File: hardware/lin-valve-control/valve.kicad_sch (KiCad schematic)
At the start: 15 parts, among them J4 Screw_Terminal_01x05, U5 TCA9534, U6 DRV8801PWP

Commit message: Add PCA9536 for the LINBus Address
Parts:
- renumbered U5 to U6, U6 to U7
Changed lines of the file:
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@@
   (symbol (lib_id "power:+3V3") (at 144.526 35.306 0) (unit 1)
     (in_bom yes) (on_board yes) (fields_autoplaced)
-    (property "Reference" "#PWR044" (id 0) (at 144.526 39.116 0)
+    (property "Reference" "#PWR047" (id 0) (at 144.526 39.116 0)
       (effects (font (size 1.27 1.27)) hide)
     )
@@
   (symbol (lib_id "Interface_Expansion:TCA9534") (at 122.047 58.293 0) (unit 1)
     (in_bom yes) (on_board yes) (fields_autoplaced)
-    (property "Reference" "U5" (id 0) (at 124.0664 41.91 0)
+    (property "Reference" "U6" (id 0) (at 124.0664 41.91 0)
       (effects (font (size 1.27 1.27)) (justify left))
     )
@@
   (symbol (lib_id "power:+3V3") (at 101.473 104.775 0) (unit 1)
     (in_bom yes) (on_board yes) (fields_autoplaced)
-    (property "Reference" "#PWR038" (id 0) (at 101.473 108.585 0)
+    (property "Reference" "#PWR041" (id 0) (at 101.473 108.585 0)
       (effects (font (size 1.27 1.27)) hide)
     )
@@
   (symbol (lib_id "power:GND") (at 155.321 126.365 0) (unit 1)
     (in_bom yes) (on_board yes) (fields_autoplaced)
-    (property "Reference" "#PWR045" (id 0) (at 155.321 132.715 0)
+    (property "Reference" "#PWR048" (id 0) (at 155.321 132.715 0)
       (effects (font (size 1.27 1.27)) hide)
     )
@@
   (symbol (lib_id "power:GND") (at 109.474 73.279 0) (unit 1)
     (in_bom yes) (on_board yes) (fields_autoplaced)
-    (property "Reference" "#PWR039" (id 0) (at 109.474 79.629 0)
+    (property "Reference" "#PWR042" (id 0) (at 109.474 79.629 0)
       (effects (font (size 1.27 1.27)) hide)
     )
@@
   (symbol (lib_id "power:GND") (at 54.102 121.285 0) (unit 1)
     (in_bom yes) (on_board yes) (fields_autoplaced)
-    (property "Reference" "#PWR036" (id 0) (at 54.102 127.635 0)
+    (property "Reference" "#PWR039" (id 0) (at 54.102 127.635 0)
       (effects (font (size 1.27 1.27)) hide)
     )
@@
   (symbol (lib_id "power:+3V3") (at 109.982 38.227 0) (unit 1)
     (in_bom yes) (on_board yes) (fields_autoplaced)
-    (property "Reference" "#PWR040" (id 0) (at 109.982 42.037 0)
+    (property "Reference" "#PWR043" (id 0) (at 109.982 42.037 0)
       (effects (font (size 1.27 1.27)) hide)
     )
@@
   (symbol (lib_id "Driver_Motor:DRV8801PWP") (at 122.428 127.381 0) (unit 1)
     (in_bom yes) (on_board yes) (fields_autoplaced)
-    (property "Reference" "U6" (id 0) (at 122.428 109.093 0))
+    (property "Reference" "U7" (id 0) (at 122.428 109.093 0))
     (property "Value" "DRV8801PWP" (id 1) (at 122.428 111.633 0))
     (property "Footprint" "Package_SO:HTSSOP-16-1EP_4.4x5mm_P0.65mm_EP3.4x5mm_Mask3x3mm_ThermalVias" (id 2) (at 152.908 113.411 0)
@@
   (symbol (lib_id "power:+3V3") (at 122.047 38.481 0) (unit 1)
     (in_bom yes) (on_board yes) (fields_autoplaced)
-    (property "Reference" "#PWR041" (id 0) (at 122.047 42.291 0)
+    (property "Reference" "#PWR044" (id 0) (at 122.047 42.291 0)
       (effects (font (size 1.27 1.27)) hide)
     )
@@
   (symbol (lib_id "power:GND") (at 122.428 151.765 0) (unit 1)
     (in_bom yes) (on_board yes) (fields_autoplaced)
-    (property "Reference" "#PWR043" (id 0) (at 122.428 158.115 0)
+    (property "Reference" "#PWR046" (id 0) (at 122.428 158.115 0)
       (effects (font (size 1.27 1.27)) hide)
     )
@@
   (symbol (lib_id "power:GND") (at 122.047 78.74 0) (unit 1)
     (in_bom yes) (on_board yes) (fields_autoplaced)
-    (property "Reference" "#PWR042" (id 0) (at 122.047 85.09 0)
+    (property "Reference" "#PWR045" (id 0) (at 122.047 85.09 0)
       (effects (font (size 1.27 1.27)) hide)
     )
@@
   (symbol (lib_id "power:GND") (at 157.353 147.066 0) (unit 1)
     (in_bom yes) (on_board yes) (fields_autoplaced)
-    (property "Reference" "#PWR046" (id 0) (at 157.353 153.416 0)
+    (property "Reference" "#PWR049" (id 0) (at 157.353 153.416 0)
       (effects (font (size 1.27 1.27)) hide)
     )
@@
   (symbol (lib_id "power:+12V") (at 96.774 107.95 0) (unit 1)
     (in_bom yes) (on_board yes) (fields_autoplaced)
-    (property "Reference" "#PWR037" (id 0) (at 96.774 111.76 0)
+    (property "Reference" "#PWR040" (id 0) (at 96.774 111.76 0)
       (effects (font (size 1.27 1.27)) hide)
     )
@@
   (symbol (lib_id "power:GND") (at 231.521 138.938 0) (unit 1)
     (in_bom yes) (on_board yes) (fields_autoplaced)
-    (property "Reference" "#PWR047" (id 0) (at 231.521 145.288 0)
-      (effects (font (size 1.27 1.27)) hide)
-    )
+    (property "Reference" "#PWR050" (id 0) (at 231.521 145.288 0)
+      (effects (font (size 1.27 1.27)) hide)
+    )

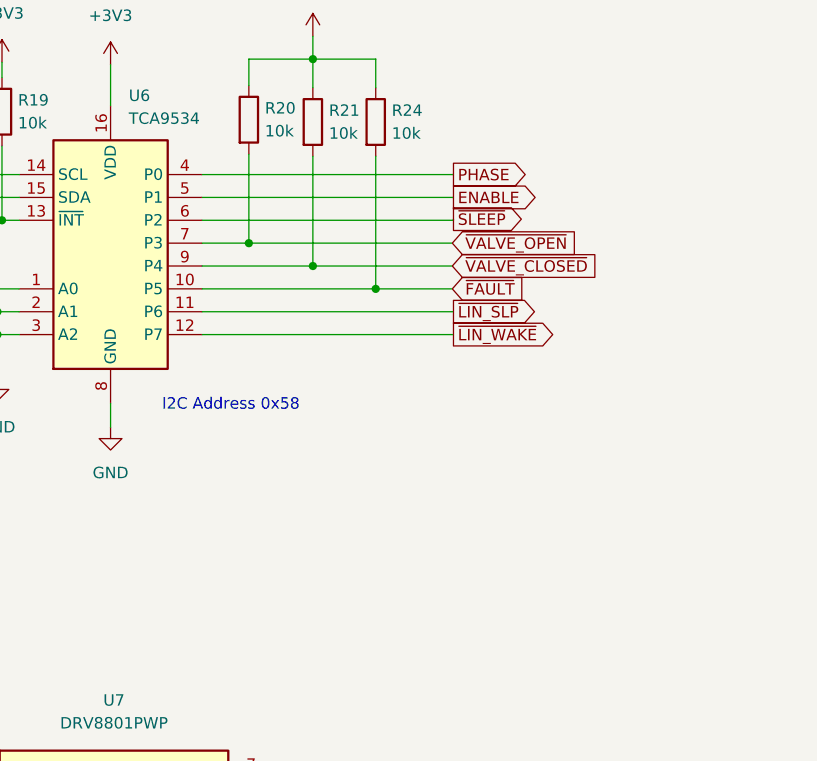
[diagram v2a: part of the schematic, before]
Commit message: Get this in place (barely) on ATTiny824.
- should not be THAT big, I thought.  Investigation to follow:

Sketch uses 7998 bytes (97%) of program storage space. Maximum is 8192 bytes.
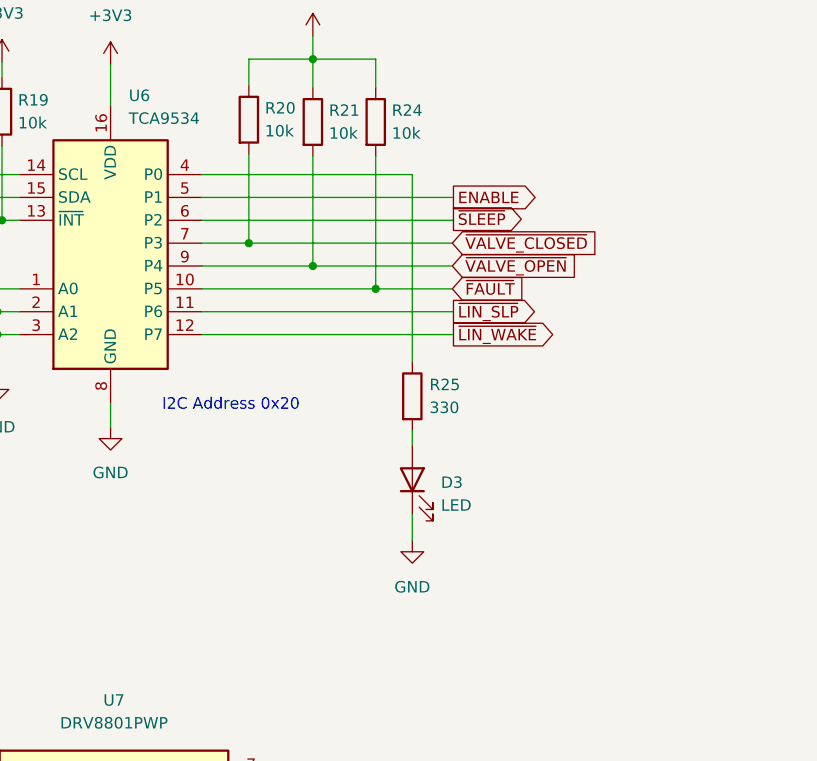
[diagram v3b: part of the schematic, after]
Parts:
- added D3: LED, LED_SMD:LED_0805_2012Metric_Pad1.15x1.40mm_HandSolder, symbol Device:LED
- added R25: 330, Resistor_SMD:R_0805_2012Metric_Pad1.20x1.40mm_HandSolder, symbol Device:R
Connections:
- net GND: now also D3.1 (K)
- net PHASE: no longer U6.4 (P0)
- net ~{VALVE_CLOSED}: now also R20.2, U6.7 (P3); no longer R21.2, U6.9 (P4)
- net ~{VALVE_OPEN}: now also R21.2, U6.9 (P4); no longer R20.2, U6.7 (P3)
- new net: R25.1, U6.4 (P0)
- new net: D3.2 (A), R25.2
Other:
- note added: "I2C Address 0x20"
- note removed: "I2C Address 0x58"
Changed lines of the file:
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@@
     (stroke (width 0) (type default) (color 0 0 0 0))
   )
-  (wire (pts (xy 132.207 50.673) (xy 160.147 50.673))
+  (wire (pts (xy 132.207 50.673) (xy 155.575 50.673))
     (stroke (width 0) (type default) (color 0 0 0 0))
   )
@@
     (stroke (width 0) (type default) (color 0 0 0 0))
   )
+  (wire (pts (xy 155.575 79.121) (xy 155.575 80.772))
+    (stroke (width 0) (type default) (color 0 0 0 0))
+  )
   (wire (pts (xy 109.982 47.498) (xy 109.982 55.753))
     (stroke (width 0) (type default) (color 0 0 0 0))
@@
     (stroke (width 0) (type default) (color 0 0 0 0))
   )
+  (wire (pts (xy 155.575 88.392) (xy 155.575 91.313))
+    (stroke (width 0) (type default) (color 0 0 0 0))
+  )
   (wire (pts (xy 42.672 117.983) (xy 42.672 119.38))
     (stroke (width 0) (type default) (color 0 0 0 0))
@@
     (stroke (width 0) (type default) (color 0 0 0 0))
   )
+  (wire (pts (xy 155.575 50.673) (xy 155.575 71.501))
+    (stroke (width 0) (type default) (color 0 0 0 0))
+  )
   (wire (pts (xy 107.823 50.673) (xy 111.887 50.673))
     (stroke (width 0) (type default) (color 0 0 0 0))
@@
     (stroke (width 0) (type default) (color 0 0 0 0))
   )
-  (text "I2C Address 0x58" (at 127.762 77.089 0)
+  (text "I2C Address 0x20" (at 127.762 77.089 0)
     (effects (font (size 1.27 1.27)) (justify left bottom))
   )
@@
     )
   )
-  (global_label "PHASE" (shape output) (at 160.147 50.673 0) (fields_autoplaced)
-    (effects (font (size 1.27 1.27)) (justify left))
-    (property "Intersheet References" "${INTERSHEET_REFS}" (id 0) (at 168.5188 50.5936 0)
-      (effects (font (size 1.27 1.27)) (justify left) hide)
-    )
-  )
-  (global_label "~{VALVE_OPEN}" (shape input) (at 160.02 58.293 0) (fields_autoplaced)
-    (effects (font (size 1.27 1.27)) (justify left))
-    (property "Intersheet References" "${INTERSHEET_REFS}" (id 0) (at 173.8347 58.2136 0)
+  (global_label "~{VALVE_CLOSED}" (shape input) (at 160.02 58.293 0) (fields_autoplaced)
+    (effects (font (size 1.27 1.27)) (justify left))
+    (property "Intersheet References" "${INTERSHEET_REFS}" (id 0) (at 176.0118 58.2136 0)
       (effects (font (size 1.27 1.27)) (justify left) hide)
     )
@@
     )
   )
-  (global_label "~{VALVE_CLOSED}" (shape input) (at 160.02 60.833 0) (fields_autoplaced)
-    (effects (font (size 1.27 1.27)) (justify left))
-    (property "Intersheet References" "${INTERSHEET_REFS}" (id 0) (at 176.0118 60.7536 0)
+  (global_label "~{VALVE_OPEN}" (shape input) (at 160.02 60.833 0) (fields_autoplaced)
+    (effects (font (size 1.27 1.27)) (justify left))
+    (property "Intersheet References" "${INTERSHEET_REFS}" (id 0) (at 173.8347 60.7536 0)
       (effects (font (size 1.27 1.27)) (justify left) hide)
     )
@@
     (pin "2")
   )
+  (symbol (lib_id "Device:R") (at 155.575 75.311 0) (unit 1)
+    (in_bom yes) (on_board yes) (fields_autoplaced)
+    (property "Reference" "R25" (id 0) (at 157.48 74.0409 0)
+      (effects (font (size 1.27 1.27)) (justify left))
+    )
+    (property "Value" "330" (id 1) (at 157.48 76.5809 0)
+      (effects (font (size 1.27 1.27)) (justify left))
+    )
+    (property "Footprint" "Resistor_SMD:R_0805_2012Metric_Pad1.20x1.40mm_HandSolder" (id 2) (at 153.797 75.311 90)
+      (effects (font (size 1.27 1.27)) hide)
+    )
+    (property "Datasheet" "~" (id 3) (at 155.575 75.311 0)
+      (effects (font (size 1.27 1.27)) hide)
+    )
+    (pin "1")
+    (pin "2")
+  )
   (symbol (lib_id "Connector:Screw_Terminal_01x05") (at 241.173 127.889 0) (unit 1)
     (in_bom yes) (on_board yes) (fields_autoplaced)
@@
     (pin "4")
     (pin "5")
+  )
+  (symbol (lib_id "Device:LED") (at 155.575 84.582 90) (unit 1)
+    (in_bom yes) (on_board yes) (fields_autoplaced)
+    (property "Reference" "D3" (id 0) (at 158.75 84.8994 90)
+      (effects (font (size 1.27 1.27)) (justify right))
+    )
+    (property "Value" "LED" (id 1) (at 158.75 87.4394 90)
+      (effects (font (size 1.27 1.27)) (justify right))
+    )
+    (property "Footprint" "LED_SMD:LED_0805_2012Metric_Pad1.15x1.40mm_HandSolder" (id 2) (at 155.575 84.582 0)
+      (effects (font (size 1.27 1.27)) hide)
+    )
+    (property "Datasheet" "~" (id 3) (at 155.575 84.582 0)
+      (effects (font (size 1.27 1.27)) hide)
+    )
+    (pin "1")
+    (pin "2")
   )
   (symbol (lib_id "power:GND") (at 54.102 121.285 0) (unit 1)
@@
     (pin "9")
   )
+  (symbol (lib_id "power:GND") (at 155.575 91.313 0) (unit 1)
+    (in_bom yes) (on_board yes) (fields_autoplaced)
+    (property "Reference" "#PWR049" (id 0) (at 155.575 97.663 0)
+      (effects (font (size 1.27 1.27)) hide)
+    )
+    (property "Value" "GND" (id 1) (at 155.575 96.52 0))
+    (property "Footprint" "" (id 2) (at 155.575 91.313 0)
+      (effects (font (size 1.27 1.27)) hide)
+    )
+    (property "Datasheet" "" (id 3) (at 155.575 91.313 0)
+      (effects (font (size 1.27 1.27)) hide)
+    )
+    (pin "1")
+  )
   (symbol (lib_id "Device:C") (at 77.597 113.792 0) (unit 1)
     (in_bom yes) (on_board yes) (fields_autoplaced)
@@
   (symbol (lib_id "power:GND") (at 157.353 147.066 0) (unit 1)
     (in_bom yes) (on_board yes) (fields_autoplaced)
-    (property "Reference" "#PWR049" (id 0) (at 157.353 153.416 0)
+    (property "Reference" "#PWR050" (id 0) (at 157.353 153.416 0)
       (effects (font (size 1.27 1.27)) hide)
     )
@@
   (symbol (lib_id "power:GND") (at 231.521 138.938 0) (unit 1)
     (in_bom yes) (on_board yes) (fields_autoplaced)
-    (property "Reference" "#PWR050" (id 0) (at 231.521 145.288 0)
-      (effects (font (size 1.27 1.27)) hide)
-    )
+    (property "Reference" "#PWR051" (id 0) (at 231.521 145.288 0)
+      (effects (font (size 1.27 1.27)) hide)
+    )

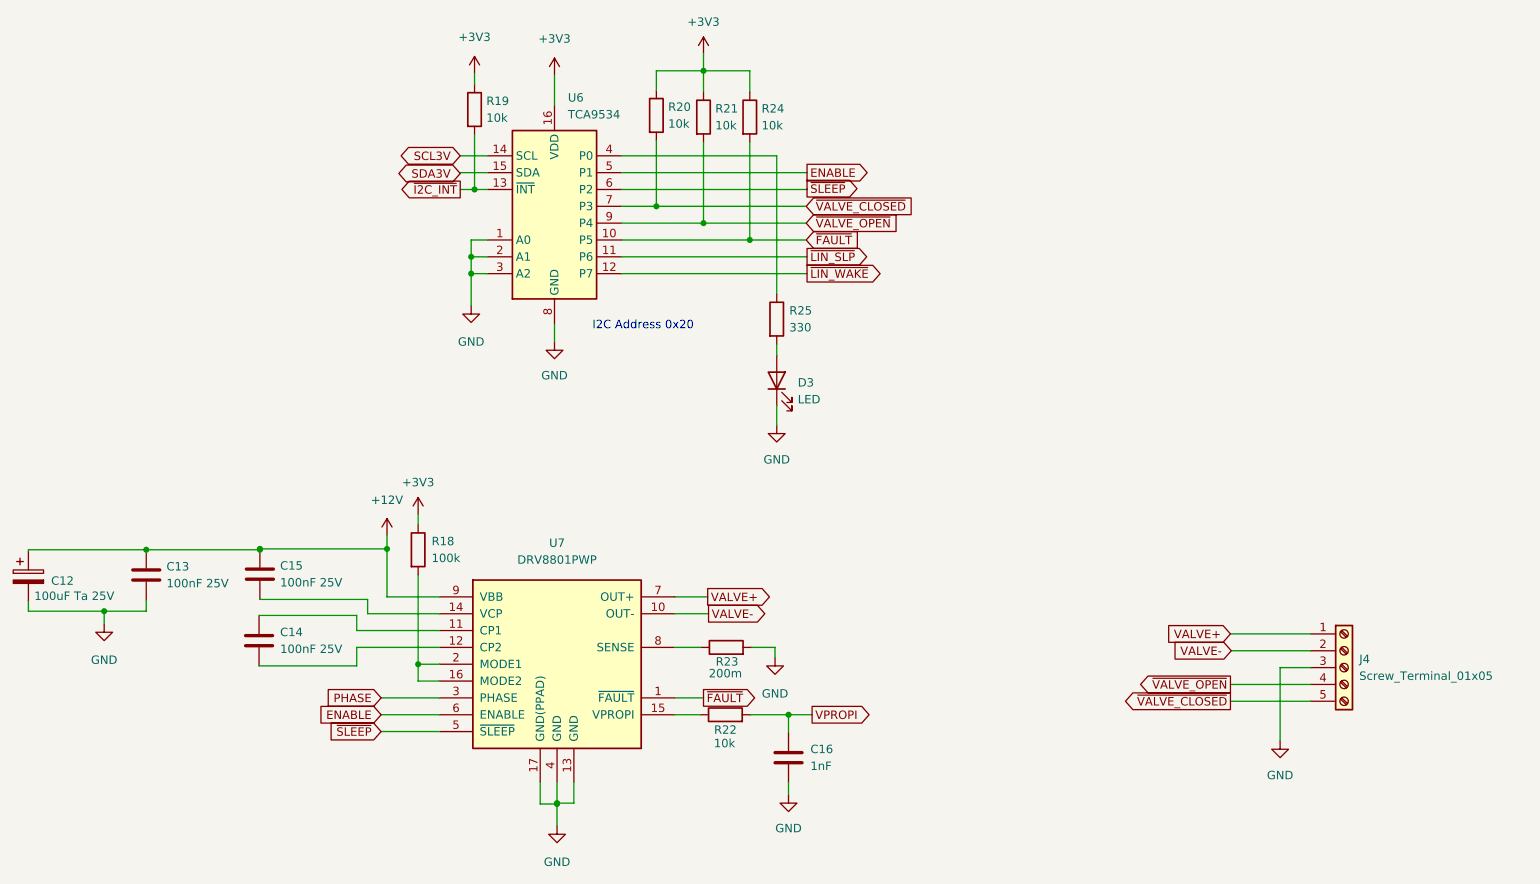
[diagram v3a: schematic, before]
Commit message: Rework valve-controller board, simplify firmware
- linbus_interface and linbus_registers moved to the common lib.
- reworked them all to compile again
- removing PCA9536 from all boards, adding the voltage reg. module
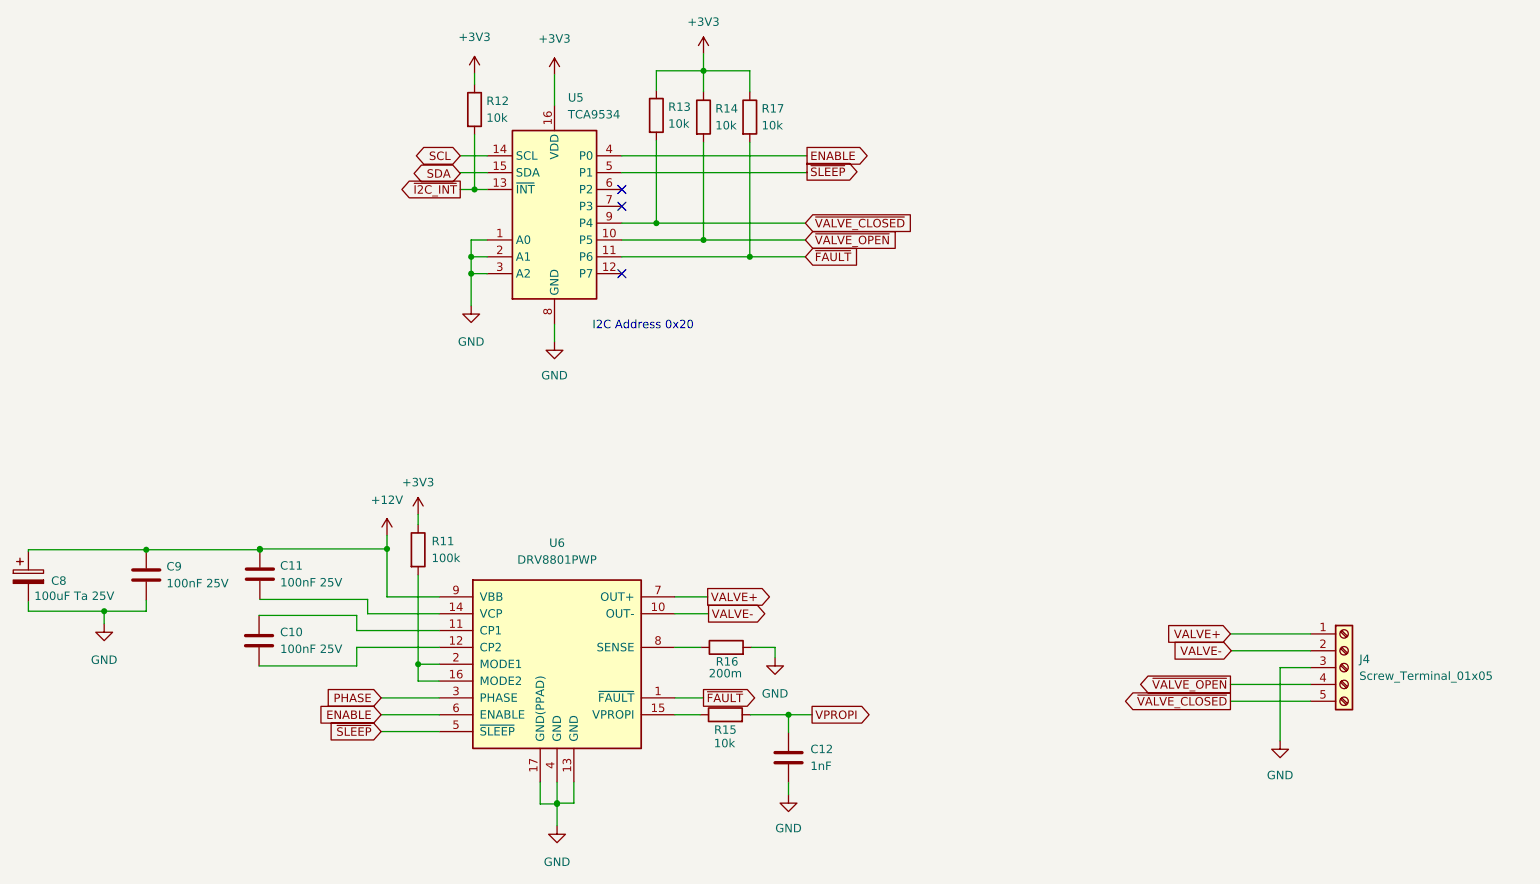
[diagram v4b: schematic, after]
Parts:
- removed D3: LED, LED_SMD:LED_0805_2012Metric_Pad1.15x1.40mm_HandSolder, symbol Device:LED
- removed R25: 330, Resistor_SMD:R_0805_2012Metric_Pad1.20x1.40mm_HandSolder, symbol Device:R
- renumbered C14 to C10, C15 to C11, C16 to C12, C12 to C8, C13 to C9, R18 to R11, R19 to R12, R20 to R13, R21 to R14, R22 to R15, R23 to R16, R24 to R17, U6 to U5, U7 to U6
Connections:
- net ~{LIN_SLP} is gone; now on net ~{FAULT}: U5.11 (P6)
- net ENABLE: now also U5.4 (P0); no longer U5.5 (P1)
- net ~{FAULT}: no longer U5.10 (P5)
- net ~{SLEEP}: now also U5.5 (P1); no longer U5.6 (P2)
- net ~{VALVE_CLOSED}: now also U5.9 (P4); no longer U5.7 (P3)
- net ~{VALVE_OPEN}: now also U5.10 (P5); no longer U5.9 (P4)
- net SCL3V renamed SCL
- net SDA3V renamed SDA
- net ~{LIN_WAKE}: no longer names the net of U5.12 (P7)
- no-connect marks 0 -> 3
